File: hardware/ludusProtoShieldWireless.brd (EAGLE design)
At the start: 59.7 x 53.3 mm, 72 parts, among them Q1 MOSFET-NCHANNELBSS138, Q2 MOSFET-NCHANNELBSS138, U1 XBEE-1XBEE-1_LOCK, U2 ARDUINO, U3 TB6612FNG

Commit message: Updates to final v1.0
Ready for reds. Reviewed by Engineering.
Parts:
- added LOGO5: SFE_LOGO_FLAME.2COP, SparkFun-Aesthetics:SFE_LOGO_FLAME_COPPER_.2
- LOGO3: value SFE_LOGO_FLAME.2EXP -> SFE_LOGO_FLAME.2_INCH; device SparkFun-Aesthetics:SFE_LOGO_FLAME_COPPER_EXPOSED_.2 -> SparkFun-Aesthetics:SFE_LOGO_FLAME_.2
- moved SJ4 11.7 mm to (5.97, 35.8)
- moved SJ3 11.7 mm to (1.52, 35.8)
- moved LOGO3 9.12 mm to (49.3, 17.1), flipped to the top, turned to 90 degrees
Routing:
- net SCL: track 36.3 -> 22.2 mm
- net SCL_I2C_PORT: track 7.02 -> 19.8 mm
- net A4: track 73.3 -> 85.1 mm
- net SDA_I2C_PORT: track 3.69 -> 15.5 mm
- net A5: track 73.2 -> 84.9 mm
- net SDA: track 38.7 -> 27.1 mm
- net BOUT2: track 21.1 -> 20.5 mm
- net XBEE_RXI: track 52.6 -> 52.1 mm
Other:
- board text added: "MOTORS"
- board text added: "V10"
- board text added: "XBEE"
- board text removed: "V02"

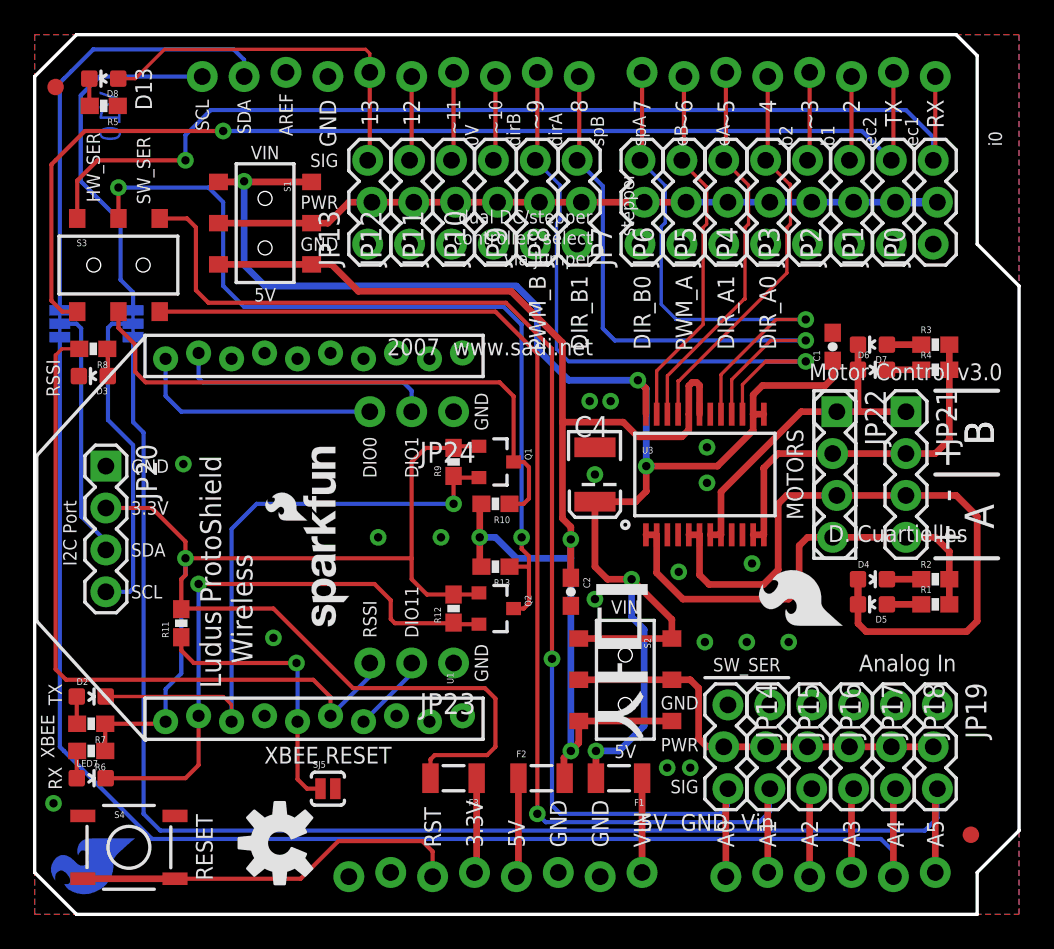
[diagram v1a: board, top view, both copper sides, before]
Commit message: Updated for QC issues for Reds
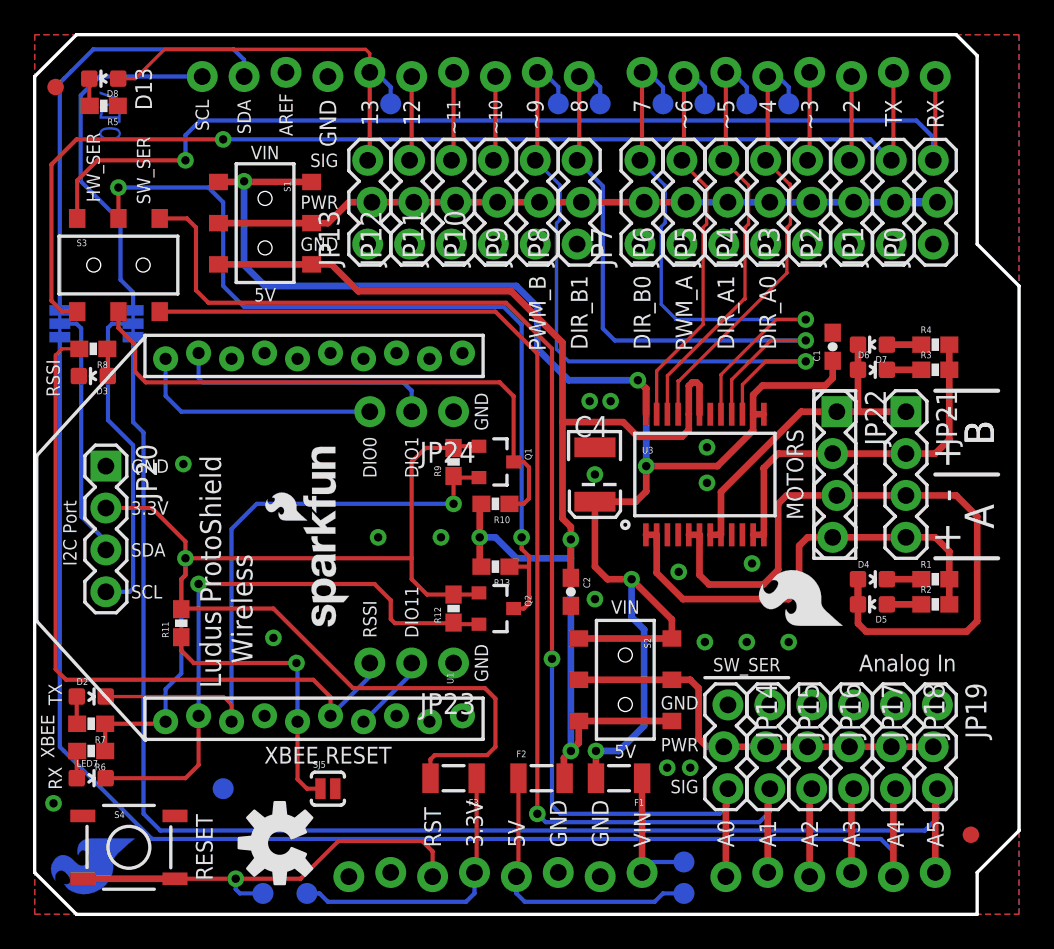
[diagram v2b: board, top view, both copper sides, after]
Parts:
- added TP1, TP10, TP11, TP12, TP2, TP3, TP4, TP5, TP6, TP7, TP8, TP9: (no value), SparkFun-Passives:PAD.03X.05
- D3: value Green -> Yellow
- F1, F2, F3: value PTCSMD -> (none)
- R1, R10, R11, R12, R13, R2, R3, R4, R6, R7, R8, R9: value 1k -> 1K
- moved R1 1.52 mm to (54.6, 20.3)
- moved R2 1.52 mm to (54.6, 18.8)
- moved R3 1.52 mm to (54.6, 33.0)
- moved R4 1.52 mm to (54.6, 34.5)
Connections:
- net 3.3V: now also TP11.P$1
- net 5V: now also TP8.P$1
- net AIN1: now also TP1.P$1
- net AIN2: now also TP2.P$1
- net BIN1: now also TP4.P$1
- net BIN2: now also TP5.P$1
- net D13: now also TP7.P$1
- net GND: now also TP9.P$1
- net N$3: now also R2.1; no longer R1.1
- net N$5: now also R1.1; no longer R2.1
- net N$8: now also R4.1; no longer R3.1
- net N$9: now also R3.1; no longer R4.1
- net PWMA: now also TP3.P$1
- net PWMB: now also TP6.P$1
- net RESET: now also TP12.P$1
- net VIN: now also TP10.P$1
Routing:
- net 3.3V: track 5.77 -> 17.6 mm
- net 5V: track 6.02 -> 17.6 mm
- net AIN1: track 24.0 -> 27.0 mm
- net VIN: track 5.72 -> 8.52 mm
- net PWMB: track 39.2 -> 41.8 mm
- net D13: track 22.6 -> 25.3 mm
- net BIN1: track 32.9 -> 35.6 mm
- net AIN2: track 23.5 -> 26.1 mm
- net PWMA: track 22.4 -> 25.0 mm
- net BIN2: track 36.1 -> 38.7 mm
- net RESET: track 23.9 -> 26.3 mm, vias 0 -> 1
- net D0/RXI: track 64.1 -> 63.6 mm
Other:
- board text removed: "0V"
- board text removed: "2007 www.sadi.net"
- board text removed: "5V GND Vin"
- board text removed: "D. Cuartielles"
- board text removed: "Motor Control v3.0"
- board text removed: "b1"
- board text removed: "b2"
- board text removed: "controller, select"
- board text removed: "dirA"
- board text removed: "dirB"
- board text removed: "dual DC/stepper"
- board text removed: "eA"
- board text removed: "eB"
- board text removed: "ec1"
- board text removed: "ec2"
- board text removed: "i0"
- board text removed: "spA"
- board text removed: "spB"
- board text removed: "stepper"
- board text removed: "via jumper"

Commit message: Moved test points around away from selective soldering points
Moved testpoints around away from selective soldering points.
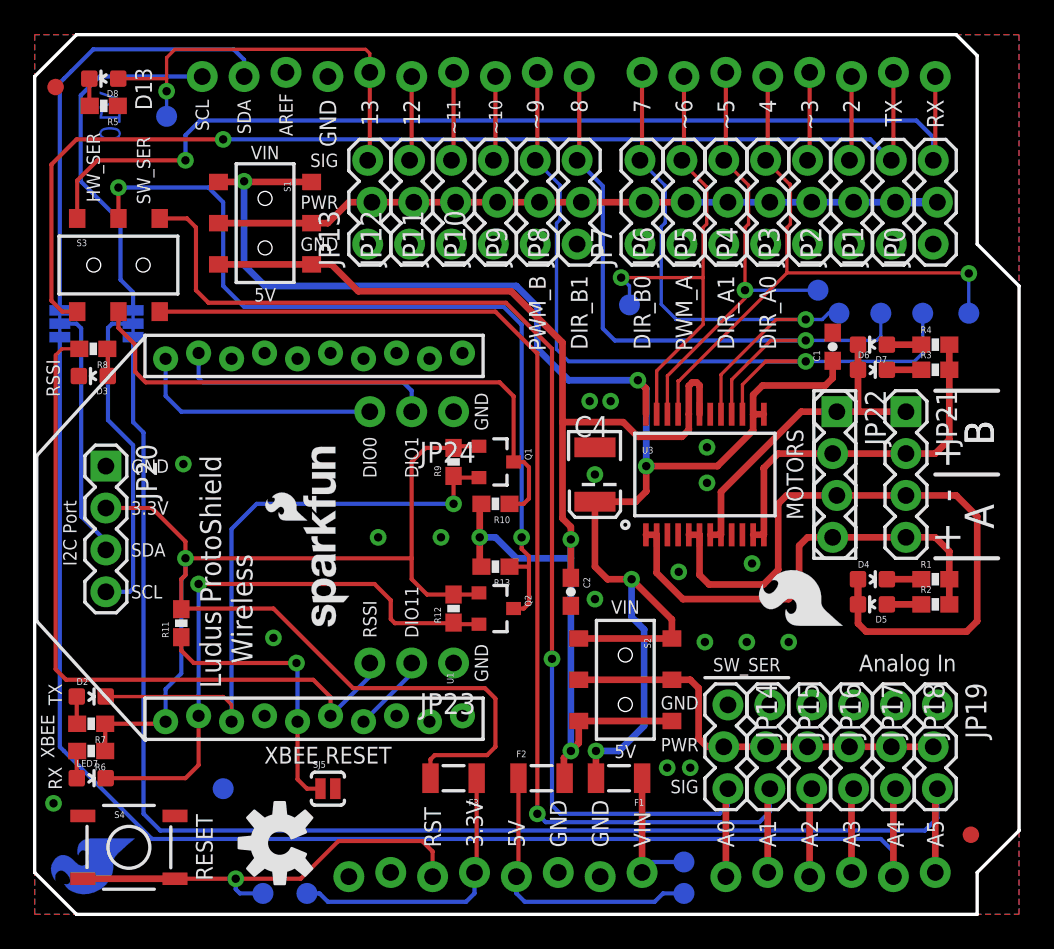
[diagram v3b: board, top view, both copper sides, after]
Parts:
- moved TP6 25.5 mm to (53.8, 36.4)
- moved TP5 21.2 mm to (51.3, 36.4)
- moved TP1 16.8 mm to (56.6, 36.4)
- moved TP4 16.6 mm to (48.8, 36.4)
- moved TP7 13.6 mm to (8.00, 48.4)
- moved TP3 13.0 mm to (36.1, 37.0)
- moved TP2 12.1 mm to (47.5, 37.8)
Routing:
- net AIN1: track 27.0 -> 37.5 mm, vias 0 -> 1
- net PWMB: track 41.8 -> 48.9 mm
- net PWMA: track 25.0 -> 29.2 mm, vias 0 -> 1
- net BIN2: track 38.7 -> 42.2 mm
- net AIN2: track 26.1 -> 28.0 mm, vias 0 -> 1
- net D13: track 25.3 -> 25.7 mm, vias 0 -> 1

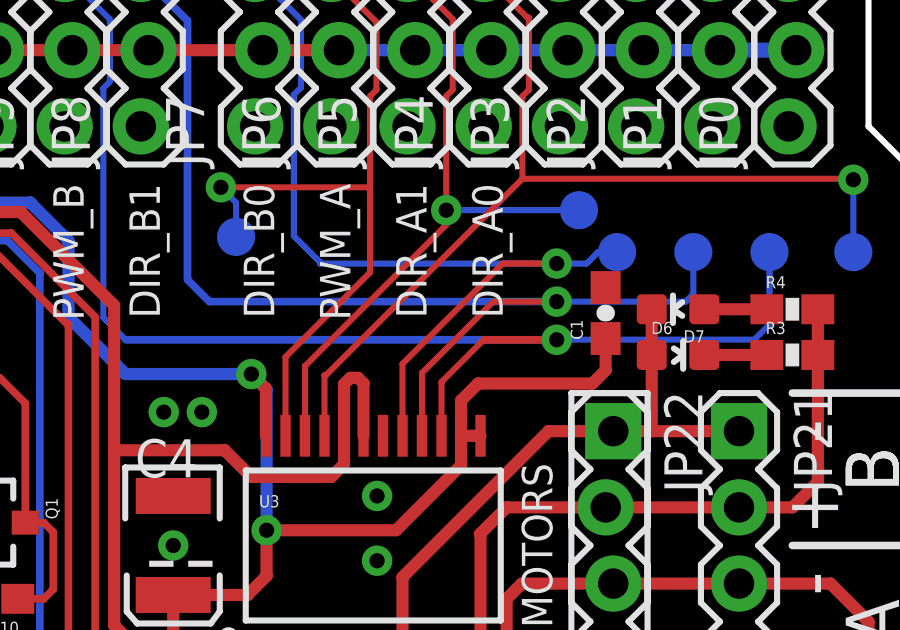
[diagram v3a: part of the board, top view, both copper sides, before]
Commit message: Updated silk images
Updated all silk images using Pete's new artwork. Bumped test point away
from header field
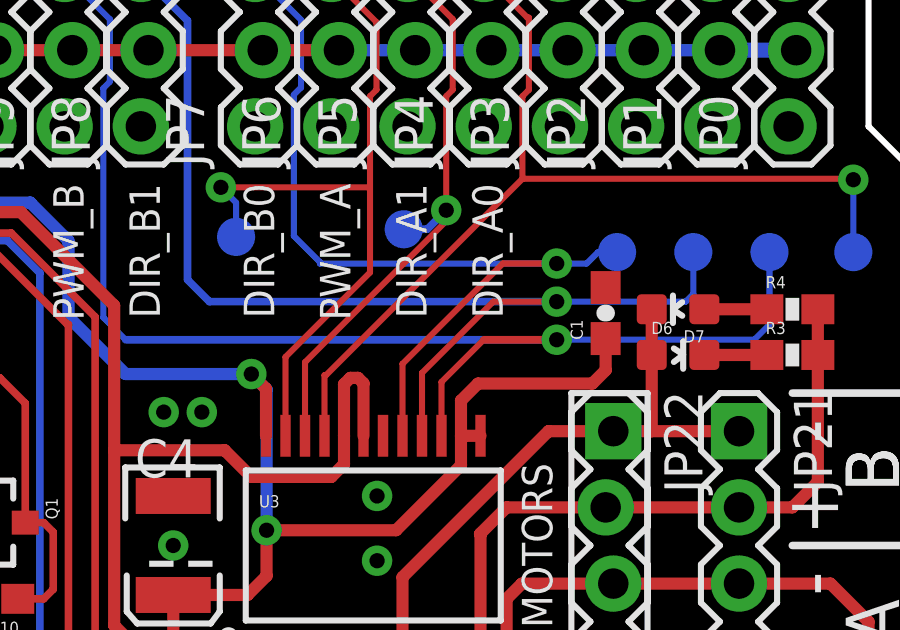
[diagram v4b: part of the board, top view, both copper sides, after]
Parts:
- moved TP2 5.88 mm to (41.7, 37.2)
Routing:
- net AIN2: track 28.0 -> 25.3 mm
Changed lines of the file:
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@@
 <setting verticaltext="up"/>
 </settings>
-<grid distance="0.02" unitdist="inch" unit="inch" style="lines" multiple="1" display="yes" altdistance="0.005" altunitdist="inch" altunit="inch"/>
+<grid distance="0.05" unitdist="inch" unit="inch" style="lines" multiple="1" display="yes" altdistance="0.005" altunitdist="inch" altunit="inch"/>
 <layers>
 <layer number="1" name="Top" color="4" fill="1" visible="yes" active="yes"/>
@@
 <element name="LOGO5" library="SparkFun-Aesthetics" package="SFE_LOGO_FLAME_COPPER_.2" value="SFE_LOGO_FLAME.2COP" x="6.35" y="4.953" rot="MR270"/>
 <element name="TP1" library="SparkFun-Passives" package="PAD.03X.05" value="" x="56.642" y="36.449" rot="MR90"/>
-<element name="TP2" library="SparkFun-Passives" package="PAD.03X.05" value="" x="47.498" y="37.846" rot="MR90"/>
+<element name="TP2" library="SparkFun-Passives" package="PAD.03X.05" value="" x="41.656" y="37.211" rot="MR90"/>
 <element name="TP3" library="SparkFun-Passives" package="PAD.03X.05" value="" x="36.068" y="36.957" rot="MR90"/>
 <element name="TP4" library="SparkFun-Passives" package="PAD.03X.05" value="" x="48.768" y="36.449" rot="MR90"/>
@@
 <contactref element="U2" pad="D5"/>
 <contactref element="JP5" pad="3"/>
-<wire x1="38.365" y1="30.326" x2="38.365" y2="32.65" width="0.2032" layer="1"/>
+<wire x1="38.365" y1="30.326" x2="38.365" y2="32.777" width="0.2032" layer="1"/>
 <wire x1="43.28795" y1="44.21505" x2="43.28795" y2="41.8592" width="0.2032" layer="1"/>
 <wire x1="43.07205" y1="41.6433" x2="43.07205" y2="37.846" width="0.2032" layer="1"/>
@@
 <wire x1="43.28795" y1="44.21505" x2="41.783" y2="45.72" width="0.2032" layer="1"/>
 <wire x1="43.07205" y1="41.6433" x2="43.28795" y2="41.8592" width="0.2032" layer="1"/>
-<wire x1="43.07205" y1="37.35705" x2="38.365" y2="32.65" width="0.2032" layer="1"/>
 <contactref element="TP2" pad="P$1"/>
 <wire x1="42.037" y1="50.927" x2="41.91" y2="51.054" width="0.254" layer="16"/>
 <via x="43.07205" y="37.846" extent="1-16" drill="0.508"/>
-<wire x1="43.07205" y1="37.846" x2="43.07205" y2="37.35705" width="0.2032" layer="1"/>
-<wire x1="47.498" y1="37.846" x2="43.07205" y2="37.846" width="0.2032" layer="16"/>
+<wire x1="41.656" y1="37.211" x2="42.43705" y2="37.211" width="0.254" layer="16"/>
+<wire x1="42.43705" y1="37.211" x2="43.07205" y2="37.846" width="0.254" layer="16"/>
+<wire x1="38.365" y1="32.777" x2="43.07205" y2="37.48405" width="0.2032" layer="1"/>
+<wire x1="43.07205" y1="37.48405" x2="43.07205" y2="37.846" width="0.2032" layer="1"/>
 </signal>
 <signal name="AIN1">

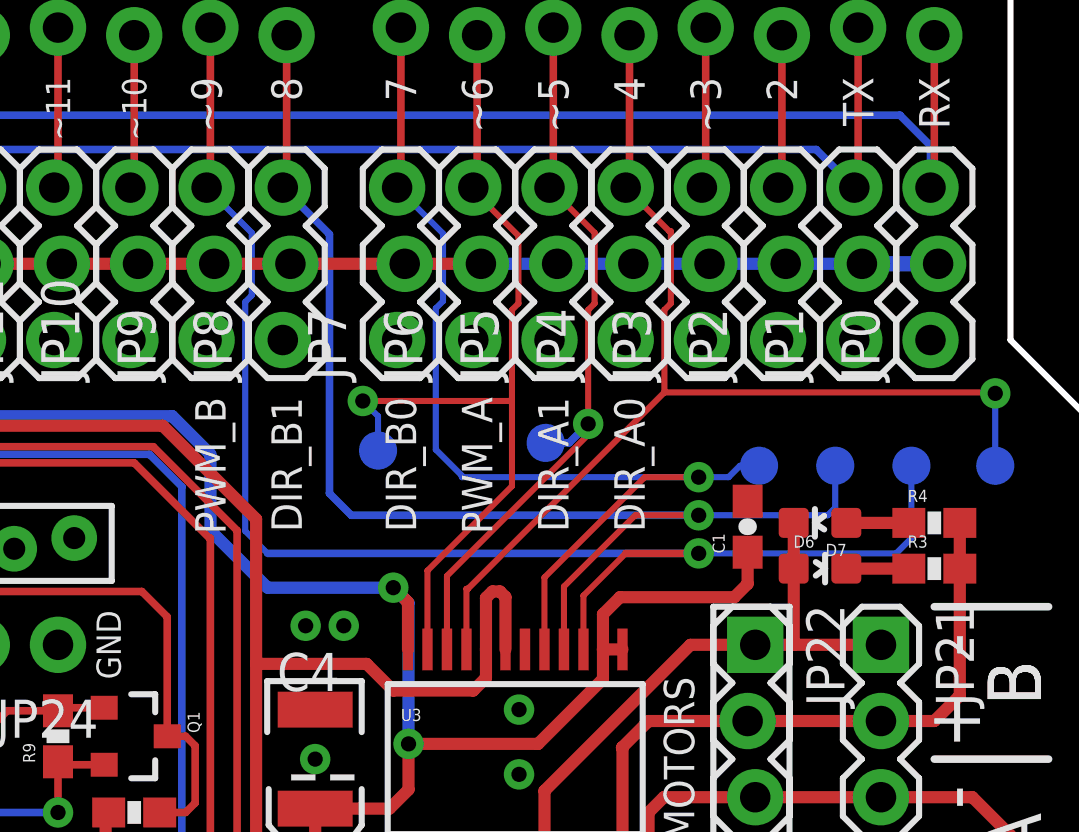
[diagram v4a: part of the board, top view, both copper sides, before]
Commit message: Moved PWM pins to 3 and 6 instead of 6 and 9
Changed the PWM control pins on the shield to pins 3 & 6 so that it is
compatible / does not conflict with the Arduino Servo library.

No test points moved. Updated silk accordingly.
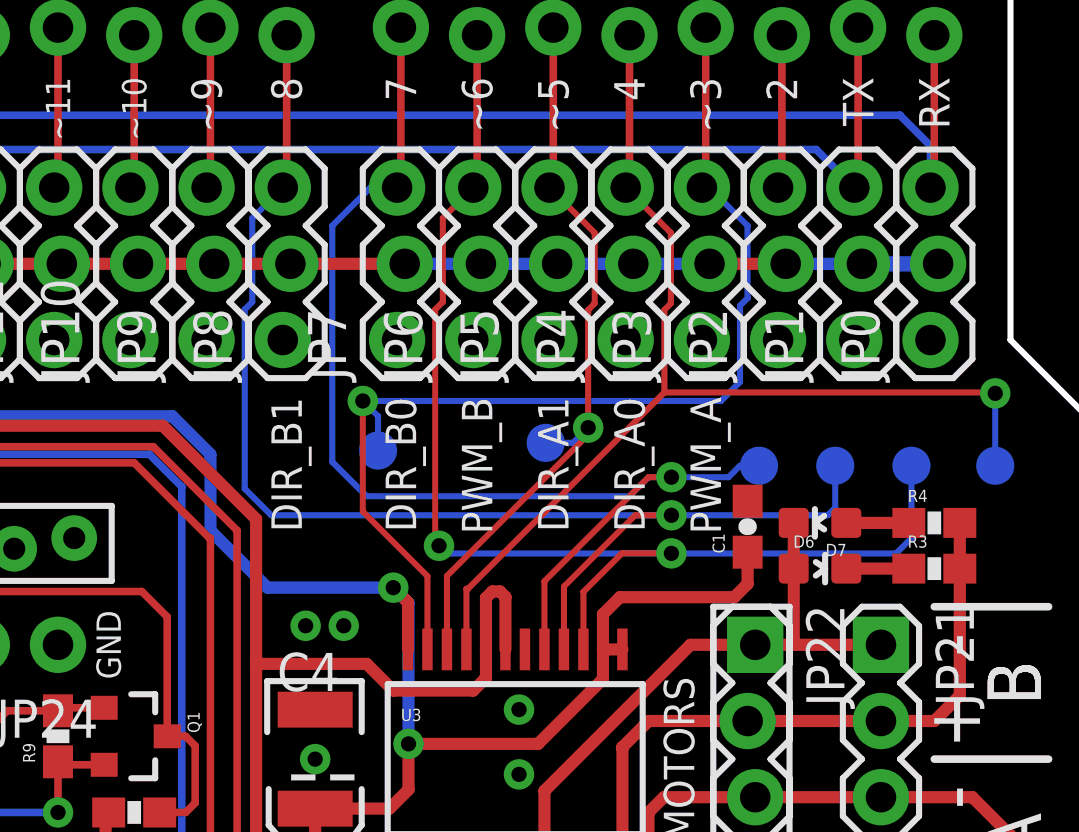
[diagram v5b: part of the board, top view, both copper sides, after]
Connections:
- removed net D3: JP3.3, U2.D3
- new net D9: JP9.3, U2.D9
- net PWMA: now also JP3.3, U2.D3; no longer JP6.3, U2.D6
- net PWMB: now also JP6.3, U2.D6; no longer JP9.3, U2.D9
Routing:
- net PWMB: track 48.9 -> 41.5 mm, vias 1 -> 2
- net PWMA: track 29.2 -> 36.6 mm
- net D3: track 5.39 -> 0.00 mm
- net D9: track 0.00 -> 5.39 mm
- net BIN1: track 35.1 -> 39.0 mm
- net BIN2: track 42.2 -> 43.9 mm
